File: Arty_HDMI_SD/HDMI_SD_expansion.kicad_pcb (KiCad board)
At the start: 4 copper layers, 109 x 40 mm, 60 parts, among them IC1 TPD8S009DSMR, J2 1140084168, J4 2000-1-2-41-00-BK, J5 UE27AC54100, U1 TPS61232DRCT, U2 MAX3421EEHJ, Y1 KX-7_12,MHz

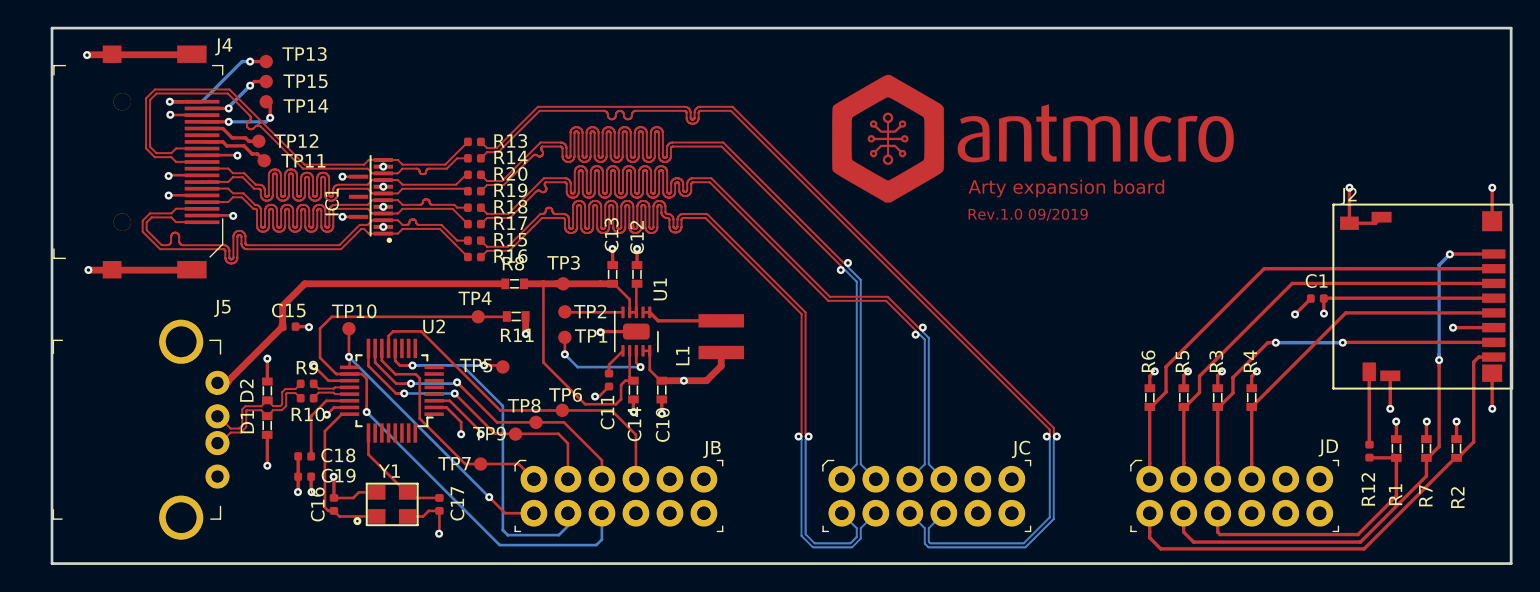
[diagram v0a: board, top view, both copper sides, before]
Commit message: Changed HDMI connector through hole
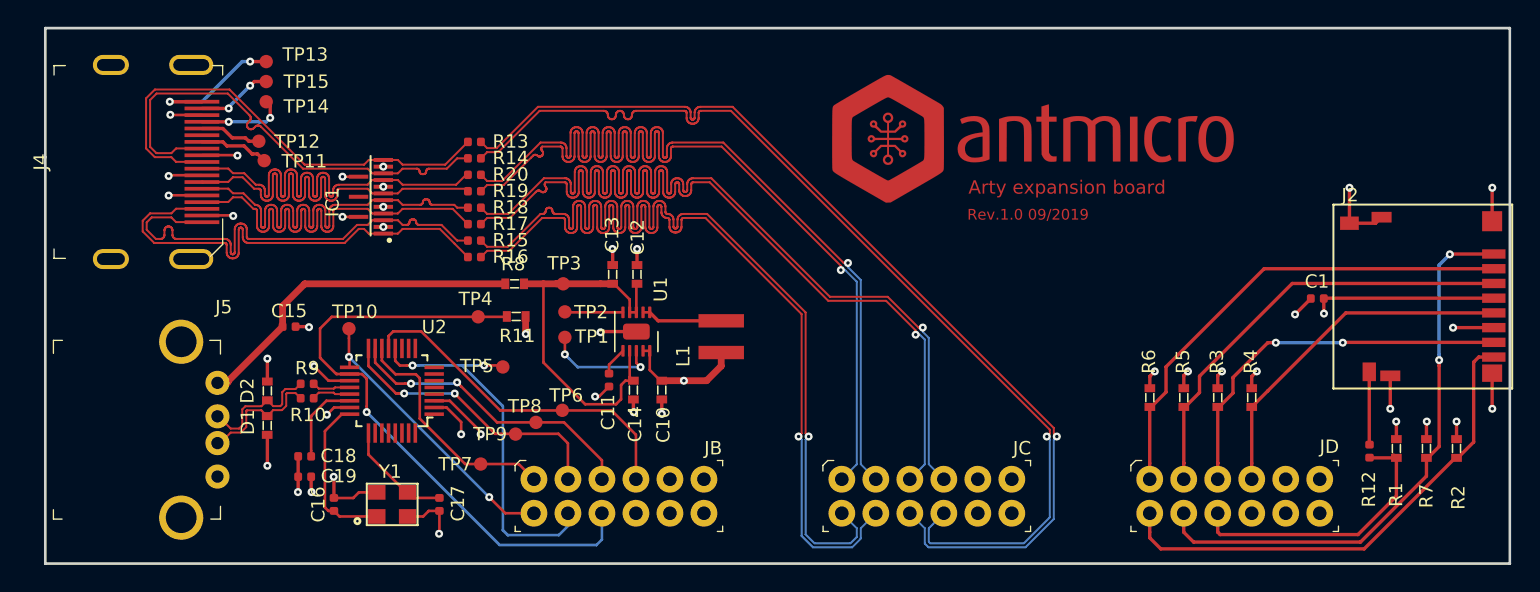
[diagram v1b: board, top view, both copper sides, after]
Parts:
- J4: value 2000-1-2-41-00-BK -> 685119134923; footprint antmicro-footprints:HDMI_A_Female_2000-1-2-41-00-BK -> antmicro-footprints:HDMI_A_Female_685119134923
- moved J4 3.15 mm to (101.6, 94.5)
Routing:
- net GND: track 78.7 -> 63.1 mm, vias 31 -> 29
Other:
- board size 109 x 40 mm -> 109.4 x 40 mm
